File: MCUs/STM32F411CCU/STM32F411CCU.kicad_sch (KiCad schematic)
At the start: 27 parts, among them J1 Conn_02x03_Odd_Even, J2 Conn_02x04_Odd_Even, SW1 SW_Push, U1 XC6206PxxxMR, U2 STM32F411CCUx, Y1 8MHz, Y2 32.768kHz

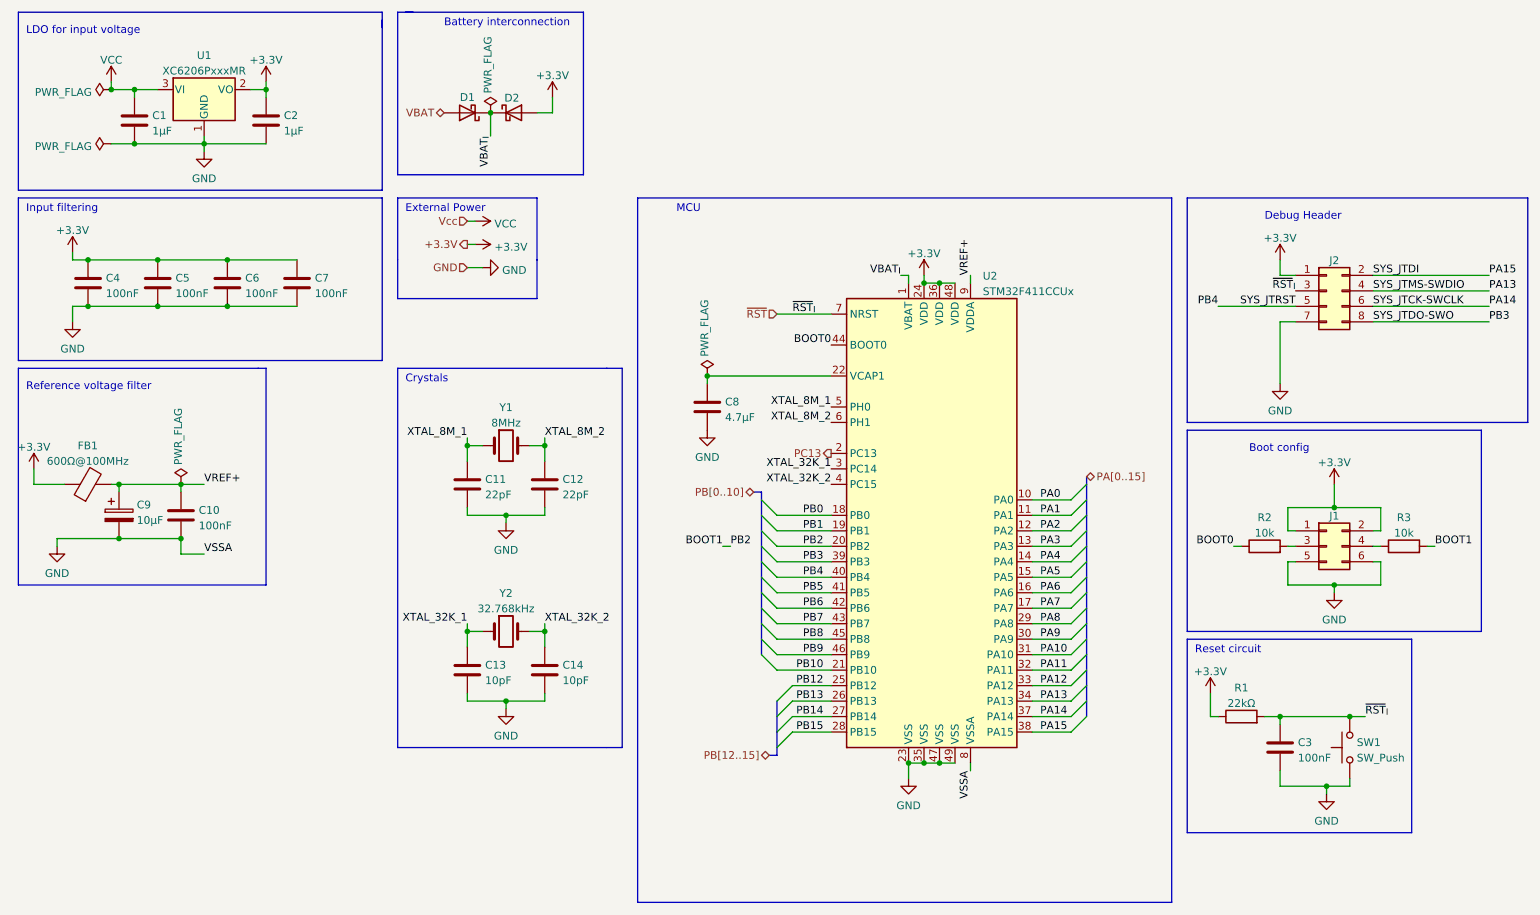
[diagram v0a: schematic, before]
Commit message: Smaller debug connector
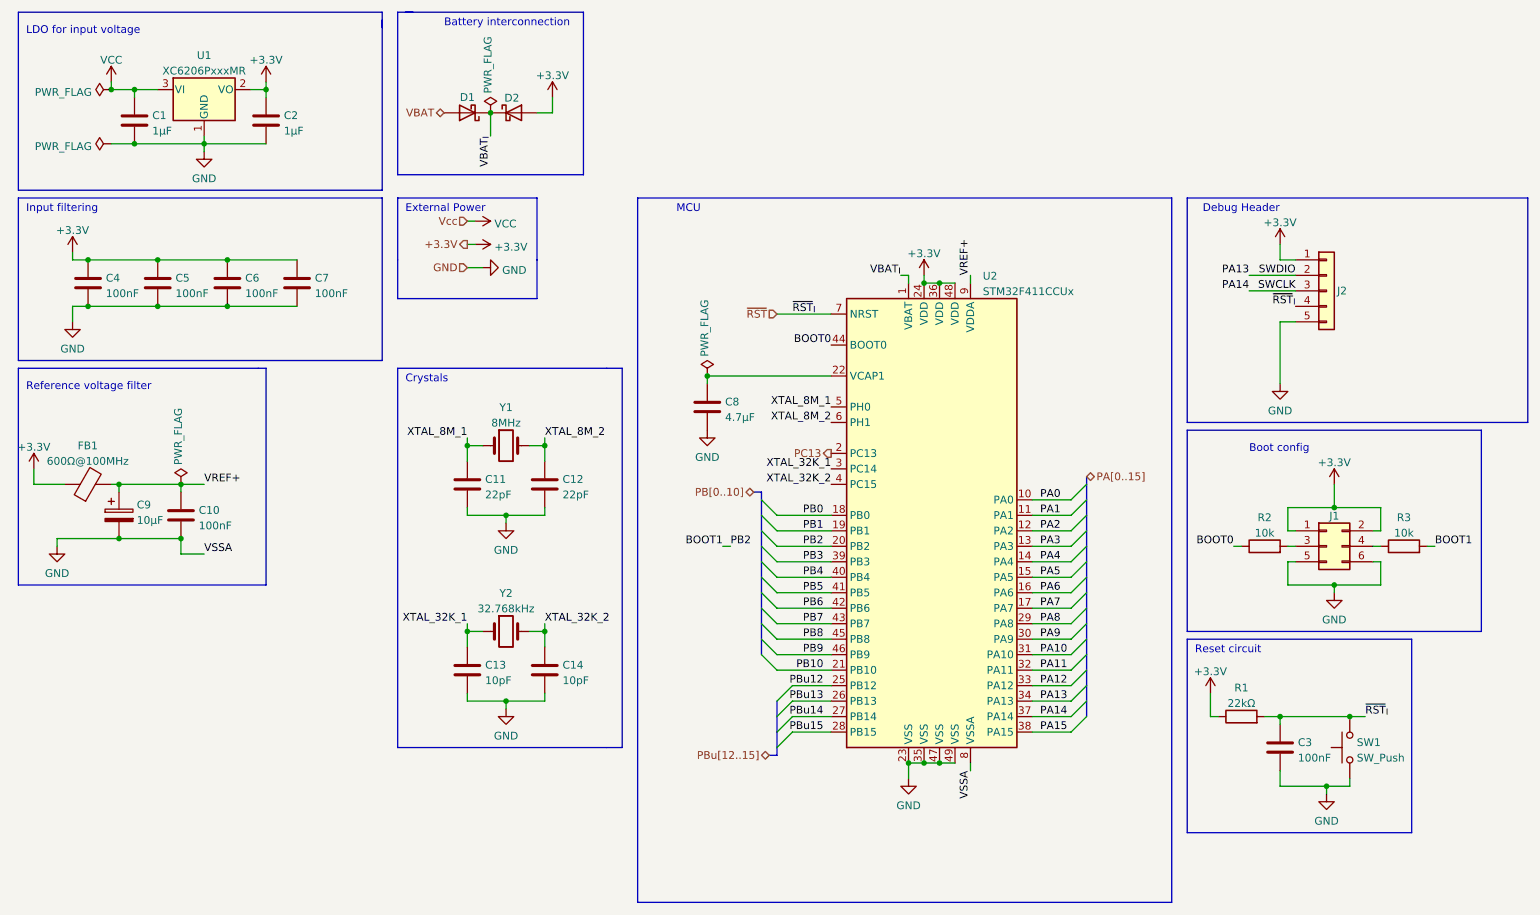
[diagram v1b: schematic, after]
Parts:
- J2: value Conn_02x04_Odd_Even -> Connector_Generic{colon}Conn_01x05; footprint Connector_PinHeader_2.54mm:PinHeader_2x04_P2.54mm_Vertical -> Connector_PinHeader_2.54mm:PinHeader_1x05_P2.54mm_Vertical; symbol Connector_Generic:Conn_02x04_Odd_Even -> Connector_Generic:Conn_01x05
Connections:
- net GND: now also J2.5 (Pin_5); no longer J2.7 (Pin_7)
- net PA13: now also J2.2 (Pin_2); no longer J2.4 (Pin_4)
- net PA14: now also J2.3 (Pin_3); no longer J2.6 (Pin_6)
- net PA15: no longer J2.2 (Pin_2)
- net PB3: no longer J2.8 (Pin_8)
- net PB4: no longer J2.5 (Pin_5)
- net ~{RST}: now also J2.4 (Pin_4); no longer J2.3 (Pin_3)
- net PB12 renamed PBu12
- net PB13 renamed PBu13
- net PB14 renamed PBu14
- net PB15 renamed PBu15

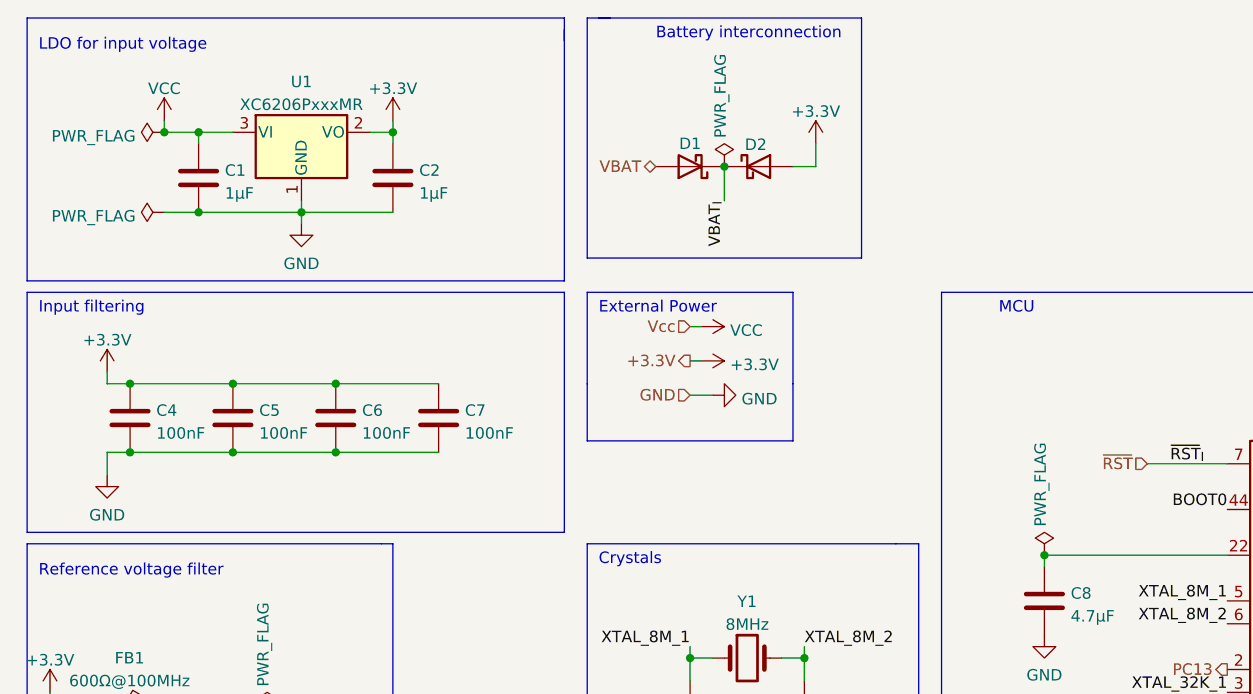
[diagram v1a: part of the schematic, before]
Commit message: STM32F411CCU: Add more filtering caps
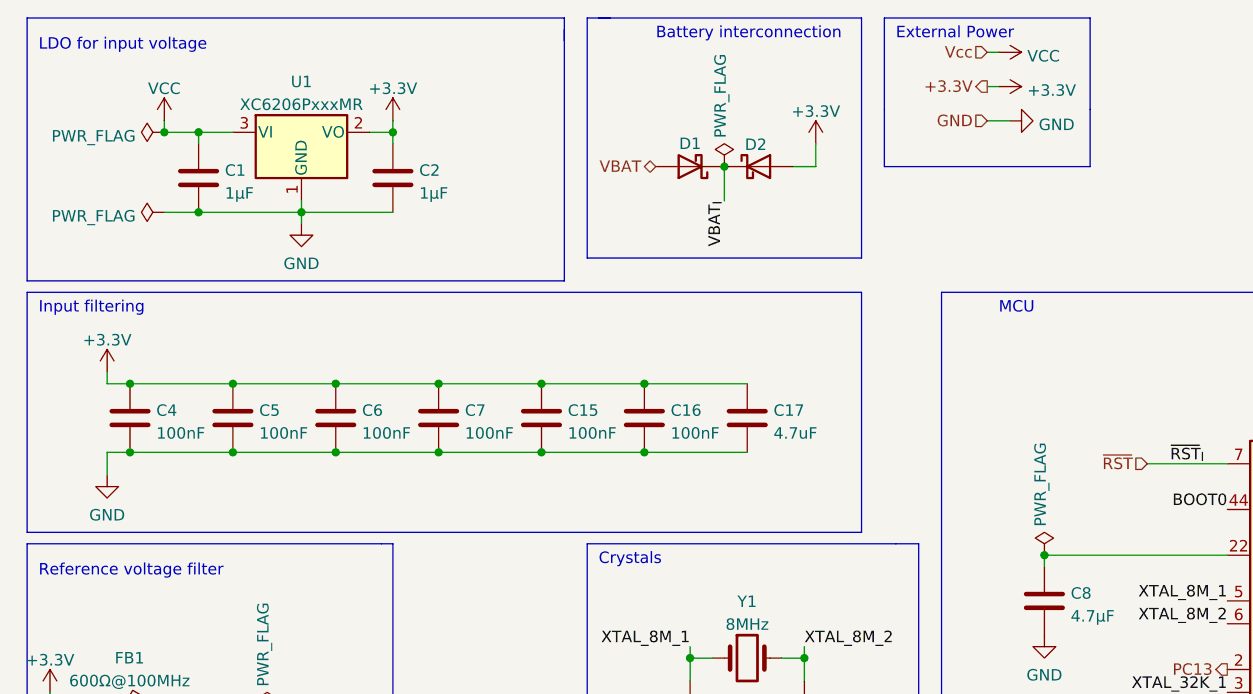
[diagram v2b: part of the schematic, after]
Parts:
- added C15, C16: 100nF, Capacitor_SMD:C_0402_1005Metric, symbol Device:C
- added C17: 4.7uF, Capacitor_SMD:C_0402_1005Metric, symbol Device:C
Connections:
- net +3V3: now also C15.1, C16.1, C17.1
- net GND: now also C15.2, C16.2, C17.2

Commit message: STM32F411CCU: Some more changes
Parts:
- added R4: 100k, Resistor_SMD:R_0402_1005Metric, symbol Device:R
- Y1: footprint Crystal:Crystal_SMD_HC49-SD -> Crystal:Crystal_SMD_5032-2Pin_5.0x3.2mm; JLCPCB C12674 -> C115962
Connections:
- net +3V3: now also R4.2
- net PA10: now also R4.1
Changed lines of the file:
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@@
+    (stroke (width 0) (type default) (color 0 0 0 0))
+  )
+  (wire (pts (xy 201.93 111.76) (xy 201.93 113.03))
+    (stroke (width 0) (type default) (color 0 0 0 0))
+  )
+  (wire (pts (xy 201.93 120.65) (xy 201.93 121.92))
     (stroke (width 0) (type default) (color 0 0 0 0))
   )
@@
     (stroke (width 0) (type default) (color 0 0 0 0))
   )
+  (wire (pts (xy 201.93 121.92) (xy 195.58 121.92))
+    (stroke (width 0) (type default) (color 0 0 0 0))
+  )
   (wire (pts (xy 46.99 105.41) (xy 46.99 102.87))
     (stroke (width 0) (type default) (color 0 0 0 0))
@@
   )
   (bus (pts (xy 142.24 111.76) (xy 142.24 109.22))
+    (stroke (width 0) (type default) (color 0 0 0 0))
+  )
+  (wire (pts (xy 195.58 121.92) (xy 193.04 121.92))
     (stroke (width 0) (type default) (color 0 0 0 0))
   )
@@
     (pin "2")
   )
+  (symbol (lib_id "Device:R") (at 201.93 116.84 180) (unit 1)
+    (in_bom yes) (on_board yes) (fields_autoplaced)
+    (property "Reference" "R4" (id 0) (at 203.708 116.0053 0)
+      (effects (font (size 1.27 1.27)) (justify right))
+    )
+    (property "Value" "100k" (id 1) (at 203.708 118.5422 0)
+      (effects (font (size 1.27 1.27)) (justify right))
+    )
+    (property "Footprint" "Resistor_SMD:R_0402_1005Metric" (id 2) (at 203.708 116.84 90)
+      (effects (font (size 1.27 1.27)) hide)
+    )
+    (property "Datasheet" "https://datasheet.lcsc.com/lcsc/2206010100_UNI-ROYAL-Uniroyal-Elec-0402WGF1003TCE_C25741.pdf" (id 3) (at 201.93 116.84 0)
+      (effects (font (size 1.27 1.27)) hide)
+    )
+    (property "JLCPCB" "C25741" (id 4) (at 201.93 116.84 90)
+      (effects (font (size 1.27 1.27)) hide)
+    )
+    (property "JLCPCB Type" "Basic" (id 5) (at 201.93 116.84 0)
+      (effects (font (size 1.27 1.27)) hide)
+    )
+    (pin "1")
+    (pin "2")
+  )
   (symbol (lib_id "Device:R") (at 247.65 104.14 90) (unit 1)
     (in_bom yes) (on_board yes) (fields_autoplaced)
@@
     (pin "2")
   )
+  (symbol (lib_id "power:+3.3V") (at 201.93 111.76 0) (unit 1)
+    (in_bom yes) (on_board yes) (fields_autoplaced)
+    (property "Reference" "#PWR0101" (id 0) (at 201.93 115.57 0)
+      (effects (font (size 1.27 1.27)) hide)
+    )
+    (property "Value" "+3.3V" (id 1) (at 201.93 108.1842 0))
+    (property "Footprint" "" (id 2) (at 201.93 111.76 0)
+      (effects (font (size 1.27 1.27)) hide)
+    )
+    (property "Datasheet" "" (id 3) (at 201.93 111.76 0)
+      (effects (font (size 1.27 1.27)) hide)
+    )
+    (pin "1")
+  )
   (symbol (lib_id "power:+3.3V") (at 215.9 128.27 0) (unit 1)
     (in_bom yes) (on_board yes) (fields_autoplaced)
@@
     (property "Reference" "Y1" (id 0) (at 100.33 81.3648 0))
     (property "Value" "8MHz" (id 1) (at 100.33 83.9017 0))
-    (property "Footprint" "Crystal:Crystal_SMD_HC49-SD" (id 2) (at 100.33 87.63 0)
-      (effects (font (size 1.27 1.27)) hide)
-    )
-    (property "Datasheet" "https://datasheet.lcsc.com/lcsc/2103291133_Yangxing-Tech-X49SM8MSD2SC_C12674.pdf" (id 3) (at 100.33 87.63 0)
-      (effects (font (size 1.27 1.27)) hide)
-    )
-    (property "JLCPCB" "C12674" (id 4) (at 100.33 87.63 0)
-      (effects (font (size 1.27 1.27)) hide)
-    )
+    (property "Footprint" "Crystal:Crystal_SMD_5032-2Pin_5.0x3.2mm" (id 2) (at 100.33 87.63 0)
+      (effects (font (size 1.27 1.27)) hide)
+    )
+    (property "Datasheet" "https://datasheet.lcsc.com/lcsc/2103291135_Yangxing-Tech-X50328MSB2GI_C115962.pdf" (id 3) (at 100.33 87.63 0)
+      (effects (font (size 1.27 1.27)) hide)
+    )
+    (property "JLCPCB" "C115962" (id 4) (at 100.33 87.63 0)
+      (effects (font (size 1.27 1.27)) hide)
+    )
